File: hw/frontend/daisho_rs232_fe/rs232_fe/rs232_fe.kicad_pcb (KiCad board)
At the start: 4 copper layers, 100 x 100 mm, 167 parts, among them J1 SAMTEC_QSH-090-D, J2 DB9, J3 DB9, J4 DB9, J5 DB9, P1 CONN_2, P10 CONN_3, P11 CONN_3, P12 CONN_3, P13 CONN_8X2, P14 CONN_3, P2 CONN_3, P3 CONN_3, P4 CONN_3, P5 CONN_3, P6 CONN_8X2, P7 CONN_2, P8 CONN_2, P9 CONN_3, Q1 MUN5212DW1, Q10 MUN5212DW1, Q11 MUN5212DW1, Q12 MUN5212DW1, Q13 MUN5212DW1, Q14 MUN5212DW1, Q15 MUN5212DW1, Q16 MUN5212DW1, Q2 MUN5212DW1, Q3 MUN5212DW1, Q4 MUN5212DW1, Q5 MUN5212DW1, Q6 MUN5212DW1, Q7 MUN5212DW1, Q8 MUN5212DW1, Q9 MUN5212DW1, U1 24C08, U2 TRSF3243, U3 TRS3237E, U4 TRSF3243, U5 TRS3237E, U6 MIC5318, U7 MIC5318

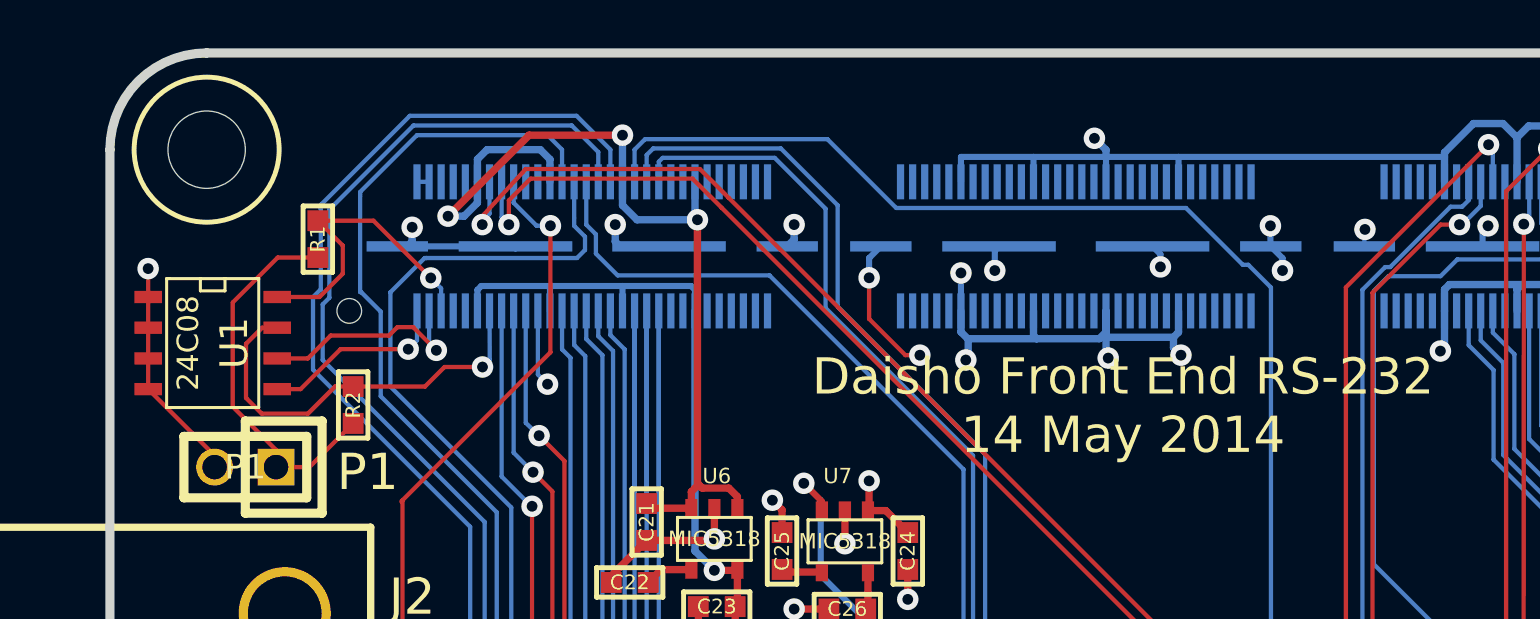
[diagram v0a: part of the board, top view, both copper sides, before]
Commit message: rs232: added resistor for VALT_FE detection, EEPROM decoupling cap
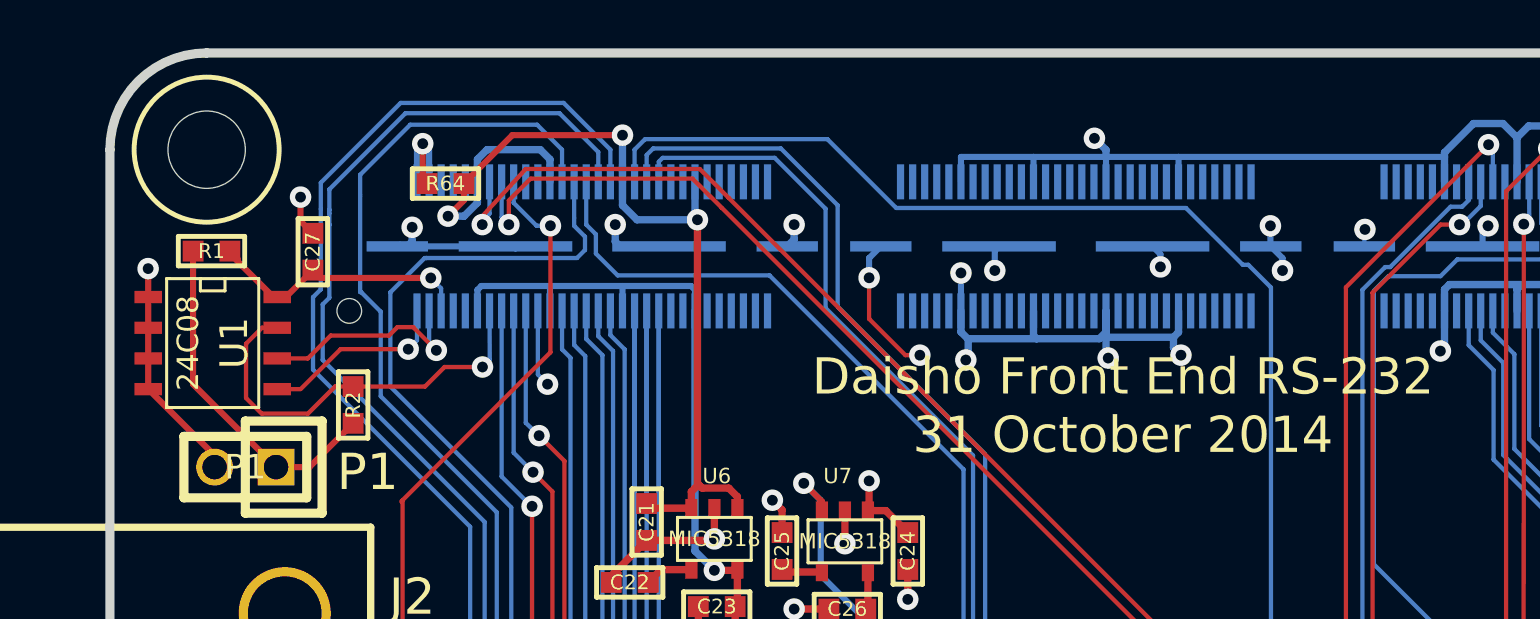
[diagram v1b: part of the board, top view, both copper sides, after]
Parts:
- added C27: 0.1uF, gsg-sm0603:GSG-0603, F.Cu at (88.4, 52.2)
- added R64: 10k, gsg-sm0603:GSG-0603, F.Cu at (93.9, 49.4)
- moved R1 4.43 mm to (84.2, 52.2), turned to 180 degrees
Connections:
- net 3V3A renamed REG_3V3
- J1 pad 10: (no net) -> Net-(J1-Pad10)
- J1 pad 100: (no net) -> Net-(J1-Pad100)
- J1 pad 101: (no net) -> Net-(J1-Pad101)
- J1 pad 102: (no net) -> Net-(J1-Pad102)
- J1 pad 103: (no net) -> Net-(J1-Pad103)
- J1 pad 104: (no net) -> Net-(J1-Pad104)
- J1 pad 105: (no net) -> Net-(J1-Pad105)
- J1 pad 106: (no net) -> Net-(J1-Pad106)
- J1 pad 109: (no net) -> Net-(J1-Pad109)
- J1 pad 110: (no net) -> Net-(J1-Pad110)
- J1 pad 111: (no net) -> Net-(J1-Pad111)
- J1 pad 112: (no net) -> Net-(J1-Pad112)
- J1 pad 113: (no net) -> Net-(J1-Pad113)
- J1 pad 114: (no net) -> Net-(J1-Pad114)
- J1 pad 115: (no net) -> Net-(J1-Pad115)
- J1 pad 116: (no net) -> Net-(J1-Pad116)
- J1 pad 117: (no net) -> Net-(J1-Pad117)
- J1 pad 118: (no net) -> Net-(J1-Pad118)
- J1 pad 119: (no net) -> Net-(J1-Pad119)
- J1 pad 120: (no net) -> Net-(J1-Pad120)
- J1 pad 121: (no net) -> Net-(J1-Pad121)
- J1 pad 122: (no net) -> Net-(J1-Pad122)
- J1 pad 123: (no net) -> Net-(J1-Pad123)
- J1 pad 124: (no net) -> Net-(J1-Pad124)
- J1 pad 125: (no net) -> Net-(J1-Pad125)
- J1 pad 126: (no net) -> Net-(J1-Pad126)
- J1 pad 127: (no net) -> Net-(J1-Pad127)
- J1 pad 128: (no net) -> Net-(J1-Pad128)
- J1 pad 129: (no net) -> Net-(J1-Pad129)
- J1 pad 130: (no net) -> Net-(J1-Pad130)
- J1 pad 133: (no net) -> Net-(J1-Pad133)
- J1 pad 134: (no net) -> Net-(J1-Pad134)
- J1 pad 141: (no net) -> Net-(J1-Pad141)
- J1 pad 142: (no net) -> Net-(J1-Pad142)
- J1 pad 163: (no net) -> Net-(J1-Pad163)
- J1 pad 164: (no net) -> Net-(J1-Pad164)
- J1 pad 165: (no net) -> Net-(J1-Pad165)
- J1 pad 166: (no net) -> Net-(J1-Pad166)
- J1 pad 169: (no net) -> Net-(J1-Pad169)
- J1 pad 170: (no net) -> Net-(J1-Pad170)
- J1 pad 171: (no net) -> Net-(J1-Pad171)
- J1 pad 172: (no net) -> Net-(J1-Pad172)
- J1 pad 173: (no net) -> Net-(J1-Pad173)
- J1 pad 174: (no net) -> Net-(J1-Pad174)
- J1 pad 175: (no net) -> Net-(J1-Pad175)
- J1 pad 176: (no net) -> Net-(J1-Pad176)
- J1 pad 177: (no net) -> Net-(J1-Pad177)
- J1 pad 178: (no net) -> Net-(J1-Pad178)
- J1 pad 179: (no net) -> Net-(J1-Pad179)
- J1 pad 180: (no net) -> Net-(J1-Pad180)
- J1 pad 19: (no net) -> Net-(J1-Pad19)
- J1 pad 21: (no net) -> Net-(J1-Pad21)
- J1 pad 43: (no net) -> Net-(J1-Pad43)
- J1 pad 44: (no net) -> Net-(J1-Pad44)
- J1 pad 45: (no net) -> Net-(J1-Pad45)
- J1 pad 46: (no net) -> Net-(J1-Pad46)
- J1 pad 49: (no net) -> Net-(J1-Pad49)
- J1 pad 5: (no net) -> Net-(J1-Pad5)
- J1 pad 50: (no net) -> Net-(J1-Pad50)
- J1 pad 51: (no net) -> Net-(J1-Pad51)
- J1 pad 52: (no net) -> Net-(J1-Pad52)
- J1 pad 53: (no net) -> Net-(J1-Pad53)
- J1 pad 54: (no net) -> Net-(J1-Pad54)
- J1 pad 55: (no net) -> Net-(J1-Pad55)
- J1 pad 56: (no net) -> Net-(J1-Pad56)
- J1 pad 57: (no net) -> Net-(J1-Pad57)
- J1 pad 58: (no net) -> Net-(J1-Pad58)
- J1 pad 59: (no net) -> Net-(J1-Pad59)
- J1 pad 60: (no net) -> Net-(J1-Pad60)
- J1 pad 61: (no net) -> Net-(J1-Pad61)
- J1 pad 62: (no net) -> Net-(J1-Pad62)
- J1 pad 63: (no net) -> Net-(J1-Pad63)
- J1 pad 64: (no net) -> Net-(J1-Pad64)
- J1 pad 65: (no net) -> Net-(J1-Pad65)
- J1 pad 66: (no net) -> Net-(J1-Pad66)
- J1 pad 67: (no net) -> Net-(J1-Pad67)
- J1 pad 68: (no net) -> Net-(J1-Pad68)
- J1 pad 69: (no net) -> Net-(J1-Pad69)
- J1 pad 7: (no net) -> Net-(J1-Pad7)
- J1 pad 70: (no net) -> Net-(J1-Pad70)
- J1 pad 73: (no net) -> Net-(J1-Pad73)
- J1 pad 74: (no net) -> Net-(J1-Pad74)
- J1 pad 75: (no net) -> Net-(J1-Pad75)
- J1 pad 76: (no net) -> Net-(J1-Pad76)
- J1 pad 77: (no net) -> Net-(J1-Pad77)
- J1 pad 78: (no net) -> Net-(J1-Pad78)
- J1 pad 79: (no net) -> Net-(J1-Pad79)
- J1 pad 8: (no net) -> Net-(J1-Pad8)
- J1 pad 80: (no net) -> Net-(J1-Pad80)
- J1 pad 81: (no net) -> Net-(J1-Pad81)
- J1 pad 82: (no net) -> Net-(J1-Pad82)
- J1 pad 85: (no net) -> Net-(J1-Pad85)
- J1 pad 86: (no net) -> Net-(J1-Pad86)
- J1 pad 87: (no net) -> Net-(J1-Pad87)
- J1 pad 88: (no net) -> Net-(J1-Pad88)
- J1 pad 89: (no net) -> Net-(J1-Pad89)
- J1 pad 9: (no net) -> Net-(J1-Pad9)
- J1 pad 90: (no net) -> Net-(J1-Pad90)
- J1 pad 91: (no net) -> Net-(J1-Pad91)
- J1 pad 92: (no net) -> Net-(J1-Pad92)
- J1 pad 93: (no net) -> Net-(J1-Pad93)
- J1 pad 94: (no net) -> Net-(J1-Pad94)
- J1 pad 97: (no net) -> Net-(J1-Pad97)
- J1 pad 98: (no net) -> Net-(J1-Pad98)
- J1 pad 99: (no net) -> Net-(J1-Pad99)
- U2 pad 20: (no net) -> Net-(U2-Pad20)
- U3 pad 16: (no net) -> Net-(U3-Pad16)
- U4 pad 20: (no net) -> Net-(U4-Pad20)
- U5 pad 16: (no net) -> Net-(U5-Pad16)
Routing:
- net /daisho_connector/VALT_FE: track 0.50 -> 5.41 mm, vias 0 -> 1
- net GND: track 157.0 -> 158.7 mm, vias 51 -> 52
- net Net-(P1-Pad1): track 15.8 -> 14.3 mm
- net /daisho_connector/VRAW_SW_5V: track 66.7 -> 68.2 mm
- net RI-B-TTL: track 109.7 -> 110.6 mm
- net RTS-B-TTL: track 96.9 -> 97.8 mm
- net CD-B-TTL: track 88.7 -> 89.4 mm
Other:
- board text added: "Daisho Front End RS-232 31 October 2014"
- board text removed: "Daisho Front End RS-232 14 May 2014"

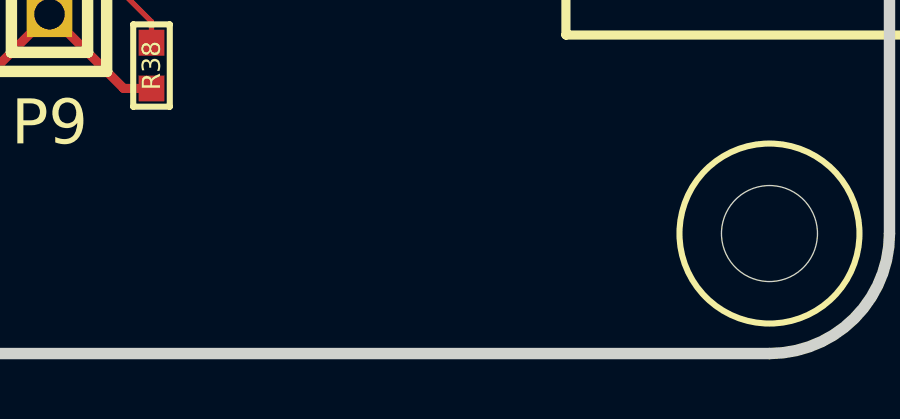
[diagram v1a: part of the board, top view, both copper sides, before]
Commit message: rs232: layer legend
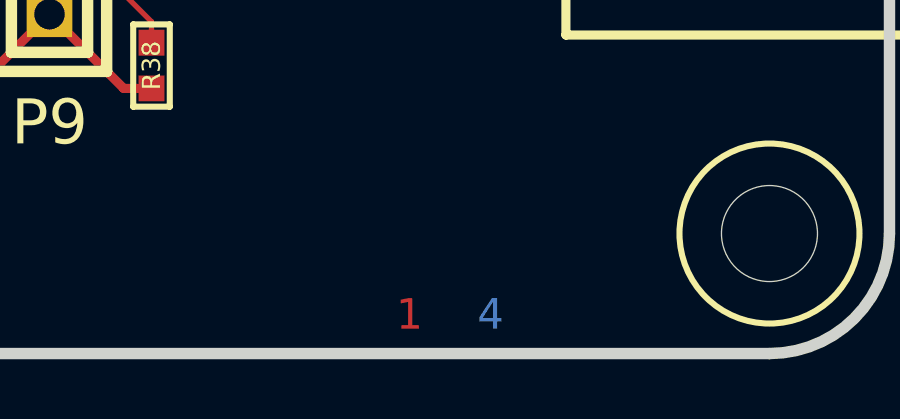
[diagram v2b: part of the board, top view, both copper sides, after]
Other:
- board text added: "1"
- board text added: "2"
- board text added: "3"
- board text added: "4"

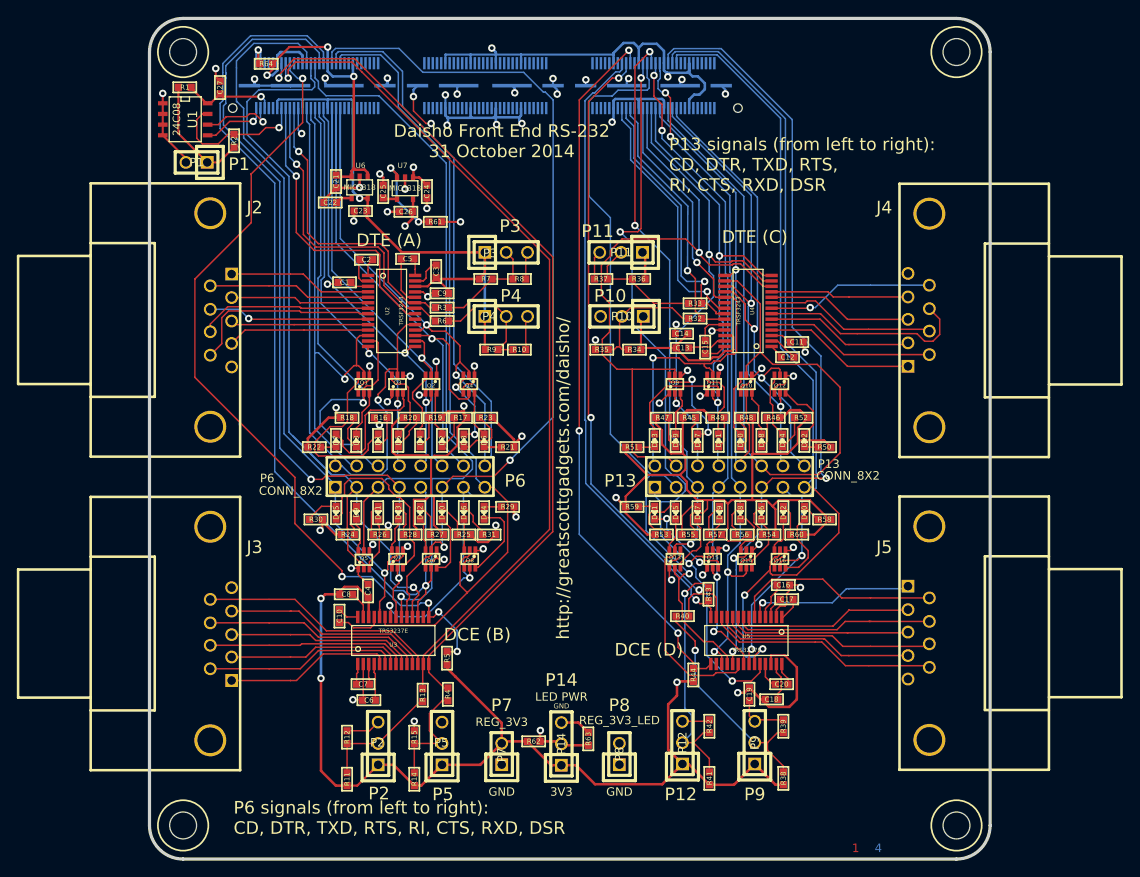
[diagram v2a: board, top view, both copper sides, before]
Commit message: rs232: moved rs232 signals from CLK to IO pins
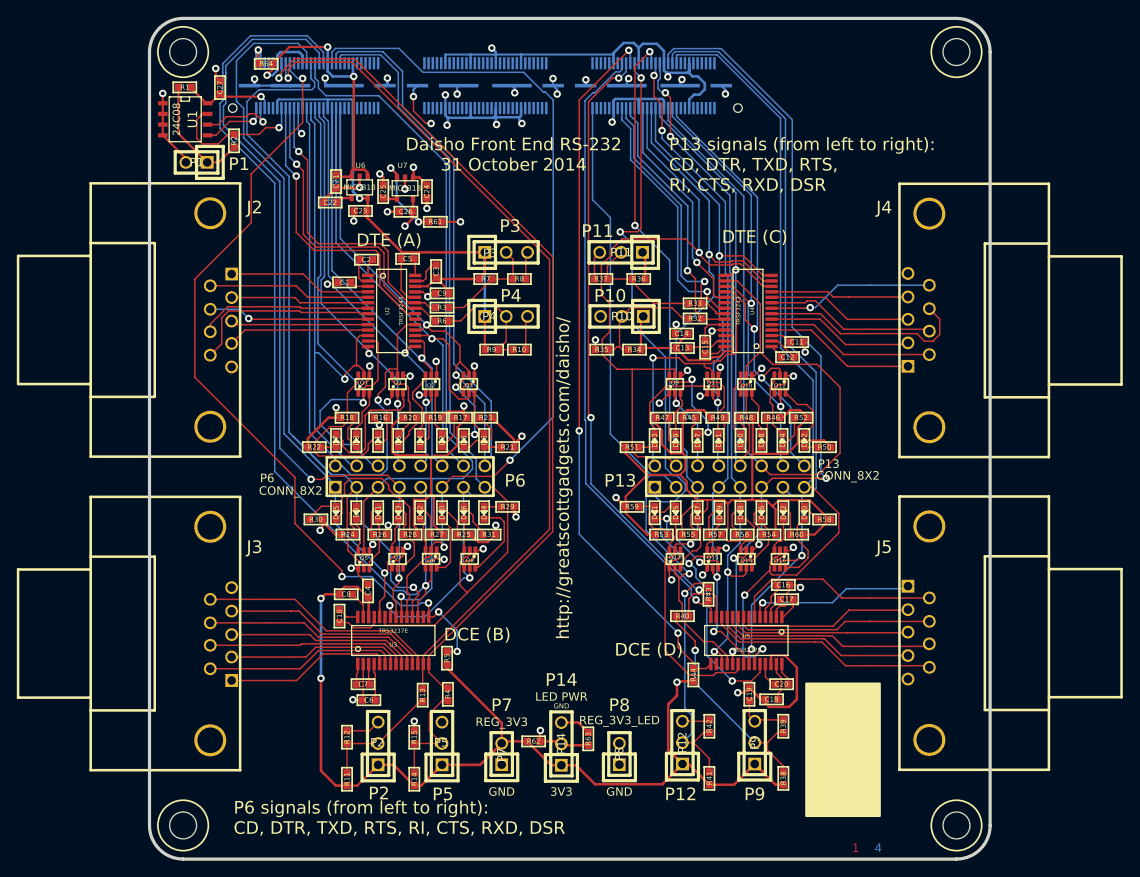
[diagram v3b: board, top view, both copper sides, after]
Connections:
- J1 pad 122: Net-(J1-Pad122) -> DTR-D-TTL
- J1 pad 141: Net-(J1-Pad141) -> CD-D-TTL
- J1 pad 145: CD-D-TTL -> Net-(J1-Pad145)
- J1 pad 147: DTR-D-TTL -> Net-(J1-Pad147)
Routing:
- net DTR-D-TTL: track 92.3 -> 80.6 mm
- net CD-D-TTL: track 95.8 -> 96.7 mm

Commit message: rs232: updated to correct QSH footprint
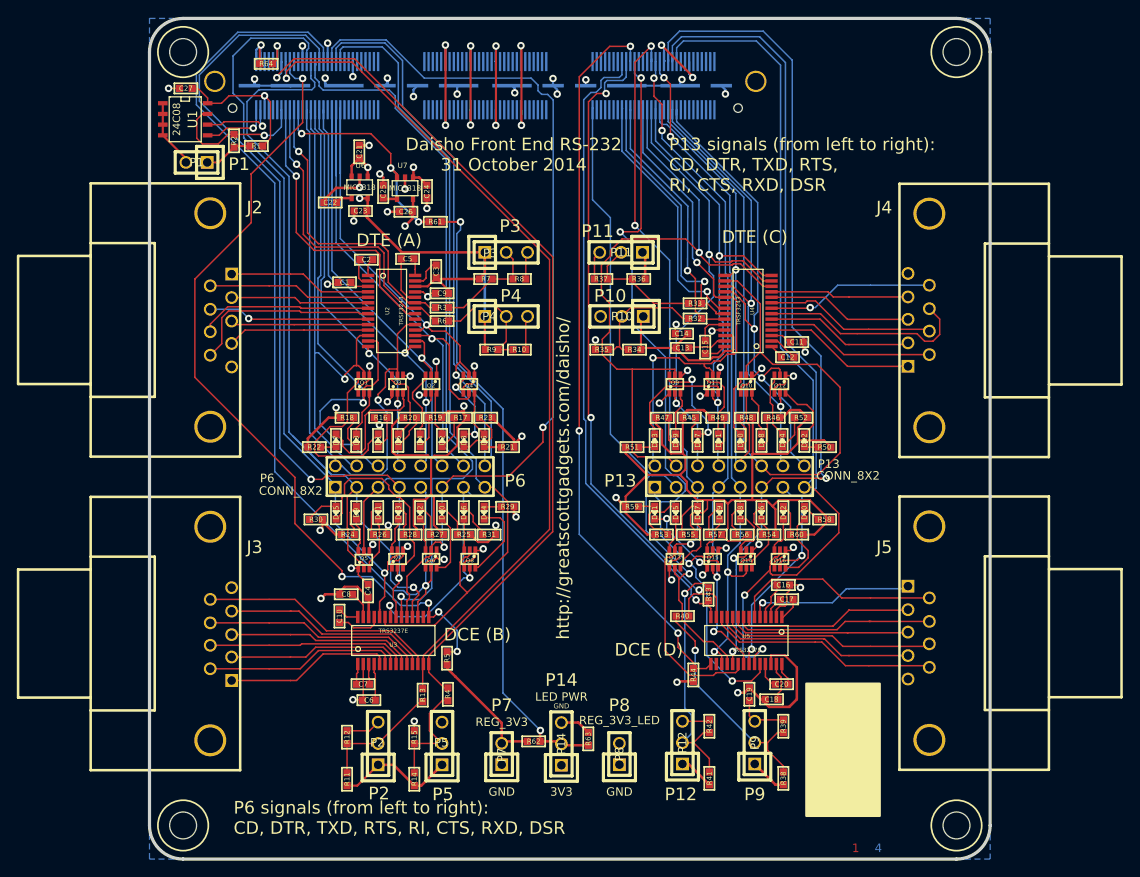
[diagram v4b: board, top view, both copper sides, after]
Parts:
- J1: footprint SAMTEC_QSH-090-01-F-D-A -> samtec_qsh-090-01-f-d-a:SAMTEC_QSH-090-01-F-D-A
- moved R1 11.0 mm to (92.7, 59.2)
- moved C21 4.48 mm to (105.0, 59.9), turned to 90 degrees
- moved C27 4.07 mm to (84.3, 52.3), turned to 180 degrees
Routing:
- net REG_3V3: track 433.5 -> 202.9 mm, vias 12 -> 14
- net /daisho_connector/VRAW_SW_5V: track 68.2 -> 19.0 mm, vias 4 -> 6
- net Net-(P1-Pad1): track 14.3 -> 6.56 mm
- net CTS-D-TTL: track 97.3 -> 104.2 mm
- net RXD-D-TTL: track 94.3 -> 101.2 mm
- net FE_I2C_VCC: track 12.9 -> 18.5 mm
- net DSR-D-TTL: track 101.3 -> 106.8 mm
- net RTS-B-TTL: track 97.8 -> 102.9 mm
- net RI-B-TTL: track 110.6 -> 114.3 mm
- net RXD-B-TTL: track 96.2 -> 99.6 mm
- net CTS-B-TTL: track 104.7 -> 107.8 mm
- net DSR-B-TTL: track 97.3 -> 100.0 mm
- net MBAUD-D-TTL: track 85.5 -> 87.9 mm
- net !EN-D-TTL: track 79.2 -> 81.5 mm
- net CD-B-TTL: track 89.4 -> 91.7 mm
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- added copper zone on Inner1.Cu, net /daisho_connector/VRAW_SW_5V
- added copper zone on B.Cu, net REG_3V3

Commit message: rs232: corrected DB9 footprints
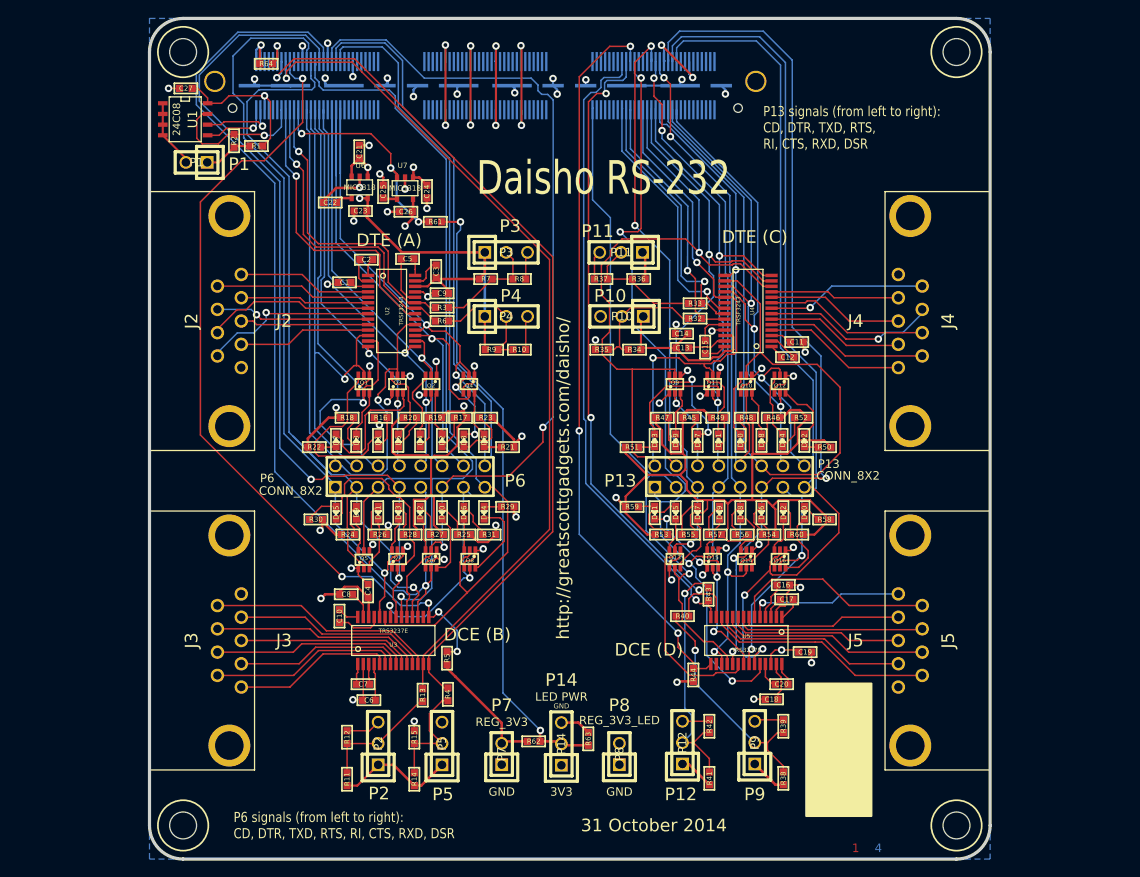
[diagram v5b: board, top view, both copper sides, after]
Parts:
- C1, C10, C11, C12, C13, C14, C15, C16, C17, C18, C19, C2, C20, C21, C22, C23, C24, C25, C26, C3, C4, C5, C6, C7, C8, C9, R1, R10, R11, R12, R13, R14, R15, R16, R17, R18, R19, R2, R20, R21, R22, R23, R24, R25, R26, R27, R28, R29, R3, R30, R31, R32, R33, R34, R35, R36, R37, R38, R39, R4, R40, R41, R42, R43, R44, R45, R46, R47, R48, R49, R5, R50, R51, R52, R53, R54, R55, R56, R57, R58, R59, R6, R60, R61, R62, R63, R7, R8, R9: footprint GSG-0603 -> gsg-sm0603:GSG-0603
- D1, D10, D11, D12, D13, D14, D15, D16, D17, D18, D19, D2, D20, D21, D22, D23, D24, D25, D26, D27, D28, D29, D3, D30, D31, D32, D4, D5, D6, D7, D8, D9: footprint GSG-0603D -> gsg-sm0603d:GSG-0603D
- H1, H2, H3, H4: footprint GSG-HOLE126MIL -> gsg-hole126mil:GSG-HOLE126MIL
- J2, J4: footprint DB9MC -> sds107:SDS107-PRW1-M09-SN63-11
- J3, J5: footprint DB9FC -> sds107:SDS107-PRP2-F09-SN13-11
- P1, P7, P8: footprint GSG-HEADER-1x2 -> gsg-header-1x2:GSG-HEADER-1x2
- P10, P11, P12, P14, P2, P3, P4, P5, P9: footprint GSG-HEADER-1x3 -> gsg-header-1x3:GSG-HEADER-1x3
- Q1, Q10, Q11, Q12, Q13, Q14, Q15, Q16, Q2, Q3, Q4, Q5, Q6, Q7, Q8, Q9: footprint GSG-SOT363 -> gsg-sot363:GSG-SOT363
- moved J5 8.56 mm to (180.0, 118.0), turned to 90 degrees
- moved J3 8.53 mm to (80.0, 118.0), turned to 270 degrees
- moved J4 8.50 mm to (180.0, 80.0), turned to 90 degrees
- moved J2 8.50 mm to (80.0, 80.0), turned to 270 degrees
- moved C19 8.31 mm to (158.0, 119.4), turned to 0 degrees
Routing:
- net REG_3V3: track 202.9 -> 192.0 mm, vias 14 -> 15
- net /rs232_pair_CD/CTS-C-232: track 25.3 -> 20.9 mm, vias 0 -> 1
- net GND: track 157.9 -> 156.5 mm, vias 50 -> 51
- net /rs232_pair_CD/RXD-D-232: track 20.7 -> 19.4 mm
- net /rs232_pair_AB/DTR-B-232: track 25.2 -> 23.9 mm
- net /rs232_pair_CD/CD-D-232: track 20.0 -> 18.7 mm
- net /rs232_pair_AB/TXD-B-232: track 22.8 -> 21.6 mm
- net /rs232_pair_AB/CTS-B-232: track 26.5 -> 25.4 mm
- net /rs232_pair_AB/RI-A-232: track 22.9 -> 21.8 mm, vias 0 -> 1
- net MBAUD-B-TTL: track 97.4 -> 98.5 mm
- net /rs232_pair_AB/RI-B-232: track 28.9 -> 27.9 mm
- net /rs232_pair_AB/CD-A-232: track 17.1 -> 16.2 mm
- net /rs232_pair_CD/RXD-C-232: track 17.6 -> 16.7 mm
- net /rs232_pair_CD/DTR-C-232: track 16.5 -> 15.7 mm
- net /rs232_pair_CD/CD-C-232: track 18.0 -> 17.2 mm
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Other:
- board text added: "31 October 2014"
- board text added: "Daisho RS-232"
- board text removed: "Daisho Front End RS-232 31 October 2014"
